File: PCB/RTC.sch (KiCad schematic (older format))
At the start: 5 parts

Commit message: Annotated Schematic
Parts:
- gave numbers to parts that had none: 5
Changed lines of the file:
@@
 $EndDescr
 $Comp
-L Timer_RTC:DS3231M U?
+L Timer_RTC:DS3231M U8
 U 1 1 5E873E81
 P 5600 4100
-F 0 "U?" H 5250 4450 50  0000 C CNN
+F 0 "U8" H 5250 4450 50  0000 C CNN
 F 1 "DS3231M" H 5600 4100 50  0000 C CNN
 F 2 "Package_SO:SOIC-16W_7.5x10.3mm_P1.27mm" H 5600 3500 50  0001 C CNN
@@
 $EndComp
 $Comp
-L Device:Battery_Cell BT?
+L Device:Battery_Cell BT2
 U 1 1 5E874DFD
 P 6000 3550
-F 0 "BT?" H 6118 3646 50  0000 L CNN
+F 0 "BT2" H 6118 3646 50  0000 L CNN
 F 1 "Battery_Cell" H 6118 3555 50  0000 L CNN
 F 2 "" V 6000 3610 50  0001 C CNN
-F 3 "~" V 6000 3610 50  0001 C CNN
+F 3 "" V 6000 3610 50  0001 C CNN
 	1    6000 3550
 	0    -1   -1   0
 $EndComp
 $Comp
-L power:GND #PWR?
+L power:GND #PWR0120
 U 1 1 5E87532F
 P 6200 3550
-F 0 "#PWR?" H 6200 3300 50  0001 C CNN
+F 0 "#PWR0120" H 6200 3300 50  0001 C CNN
 F 1 "GND" H 6205 3377 50  0000 C CNN
 F 2 "" H 6200 3550 50  0001 C CNN
@@
 $EndComp
 $Comp
-L power:+3.3V #PWR?
+L power:+3.3V #PWR0118
 U 1 1 5E875558
 P 5500 3650
-F 0 "#PWR?" H 5500 3500 50  0001 C CNN
+F 0 "#PWR0118" H 5500 3500 50  0001 C CNN
 F 1 "+3.3V" H 5515 3823 50  0000 C CNN
 F 2 "" H 5500 3650 50  0001 C CNN
@@
 NoConn ~ 6100 3900
 $Comp
-L power:GND #PWR?
+L power:GND #PWR0119
 U 1 1 5E878241
 P 5600 4550
-F 0 "#PWR?" H 5600 4300 50  0001 C CNN
+F 0 "#PWR0119" H 5600 4300 50  0001 C CNN
 F 1 "GND" H 5605 4377 50  0000 C CNN
 F 2 "" H 5600 4550 50  0001 C CNN
@@
 SCL
 $Comp
-L Device:C_Small C?
+L Device:C_Small C43
 U 1 1 5E879AEF
 P 5500 2750
-F 0 "C?" H 5592 2796 50  0000 L CNN
+F 0 "C43" H 5592 2796 50  0000 L CNN
 F 1 "1uF" H 5592 2705 50  0000 L CNN
 F 2 "" H 5500 2750 50  0001 C CNN
-F 3 "~" H 5500 2750 50  0001 C CNN
+F 3 "" H 5500 2750 50  0001 C CNN
 	1    5500 2750
 	1    0    0    -1
 $EndComp
 $Comp
-L power:+3.3V #PWR?
+L power:+3.3V #PWR0116
 U 1 1 5E879CC5
 P 5500 2600
-F 0 "#PWR?" H 5500 2450 50  0001 C CNN
+F 0 "#PWR0116" H 5500 2450 50  0001 C CNN
 F 1 "+3.3V" H 5515 2773 50  0000 C CNN
 F 2 "" H 5500 2600 50  0001 C CNN
@@
 	5500 2600 5500 2650
 $Comp
-L power:GND #PWR?
+L power:GND #PWR0117
 U 1 1 5E87A00D
 P 5500 2900
-F 0 "#PWR?" H 5500 2650 50  0001 C CNN
+F 0 "#PWR0117" H 5500 2650 50  0001 C CNN
 F 1 "GND" H 5505 2727 50  0000 C CNN
 F 2 "" H 5500 2900 50  0001 C CNN
@@
 	5500 2850 5500 2900
 $Comp
-L Device:R_Small R?
+L Device:R_Small R22
 U 1 1 5E87BE49
 P 4950 4300
-F 0 "R?" V 5054 4300 50  0000 C CNN
+F 0 "R22" V 5054 4300 50  0000 C CNN
 F 1 "10k" V 5145 4300 50  0000 C CNN
 F 2 "" H 4950 4300 50  0001 C CNN
-F 3 "~" H 4950 4300 50  0001 C CNN
+F 3 "" H 4950 4300 50  0001 C CNN
 	1    4950 4300
 	0    1    1    0
 $EndComp
 $Comp
-L power:+3.3V #PWR?
+L power:+3.3V #PWR0115
 U 1 1 5E87C09D
 P 4800 4250
-F 0 "#PWR?" H 4800 4100 50  0001 C CNN
+F 0 "#PWR0115" H 4800 4100 50  0001 C CNN
 F 1 "+3.3V" H 4815 4423 50  0000 C CNN
 F 2 "" H 4800 4250 50  0001 C CNN
@@
 	5050 4300 5100 4300
 $Comp
-L Device:R_Small R?
+L Device:R_Small R23
 U 1 1 5E87E241
 P 6250 4000
-F 0 "R?" V 6354 4000 50  0000 C CNN
+F 0 "R23" V 6354 4000 50  0000 C CNN
 F 1 "10k" V 6445 4000 50  0000 C CNN
 F 2 "" H 6250 4000 50  0001 C CNN
-F 3 "~" H 6250 4000 50  0001 C CNN
+F 3 "" H 6250 4000 50  0001 C CNN
 	1    6250 4000
 	1    0    0    1
 $EndComp
 $Comp
-L power:+3.3V #PWR?
+L power:+3.3V #PWR0121
 U 1 1 5E87E247
 P 6250 3850
-F 0 "#PWR?" H 6250 3700 50  0001 C CNN
+F 0 "#PWR0121" H 6250 3700 50  0001 C CNN
 F 1 "+3.3V" H 6265 4023 50  0000 C CNN
 F 2 "" H 6250 3850 50  0001 C CNN

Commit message: Added Dielectric and voltage rating to all capacitors
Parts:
- C43: Dielectric (none) -> X7R; Voltage Rating (none) -> 6.3V
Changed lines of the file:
@@
 $Descr A4 11693 8268
 encoding utf-8
-Sheet 13 20
+Sheet 15 20
 Title ""
 Date ""
@@
 F 2 "" H 5500 2750 50  0001 C CNN
 F 3 "" H 5500 2750 50  0001 C CNN
+F 4 "X7R" H 5500 2750 50  0001 C CNN "Dielectric"
+F 5 "6.3V" H 5500 2750 50  0001 C CNN "Voltage Rating"
 	1    5500 2750
 	1    0    0    -1

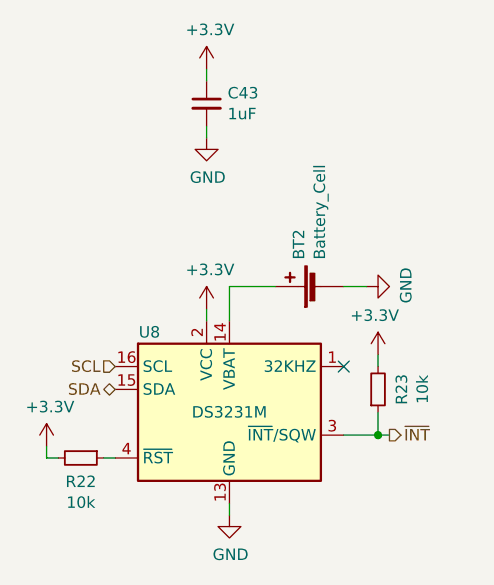
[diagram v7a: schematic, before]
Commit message: Named elements with missing values
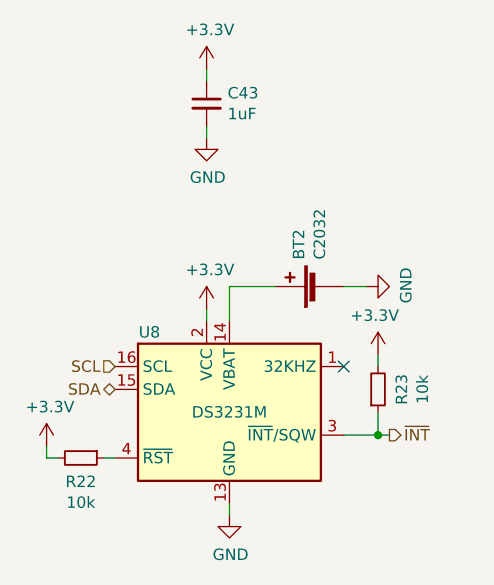
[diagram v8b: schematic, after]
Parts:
- BT2: value Battery_Cell -> C2032
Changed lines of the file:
@@
 P 6000 3550
 F 0 "BT2" H 6118 3646 50  0000 L CNN
-F 1 "Battery_Cell" H 6118 3555 50  0000 L CNN
+F 1 "C2032" H 6118 3555 50  0000 L CNN
 F 2 "" V 6000 3610 50  0001 C CNN
 F 3 "" V 6000 3610 50  0001 C CNN
